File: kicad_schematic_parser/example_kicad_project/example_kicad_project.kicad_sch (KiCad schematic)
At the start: 0 parts

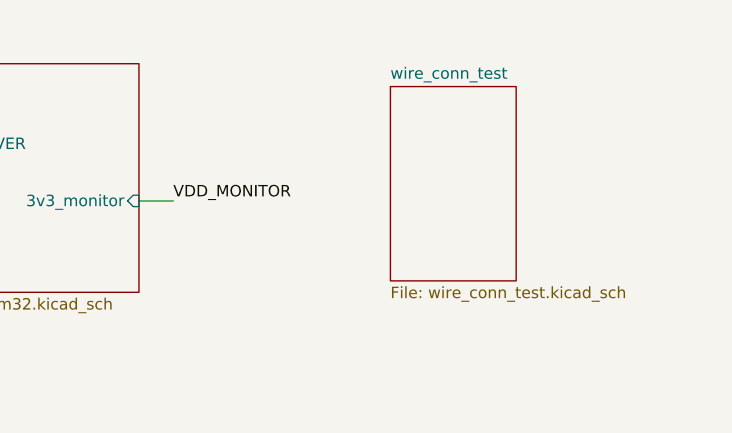
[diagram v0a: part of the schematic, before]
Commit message: sheets detecting component connections to pins
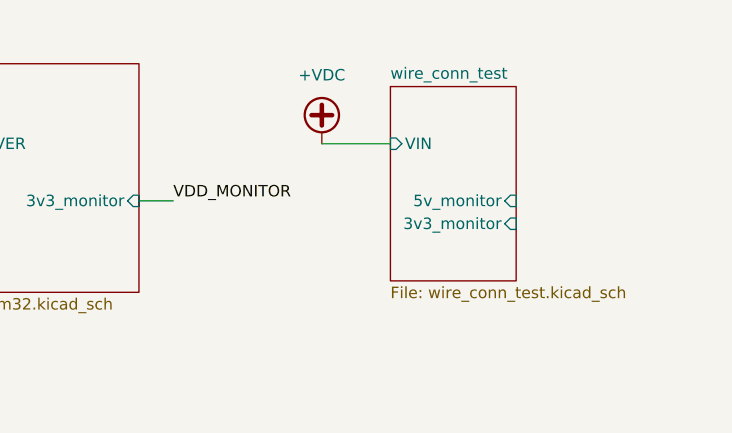
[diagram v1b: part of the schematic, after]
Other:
- sheet wire_conn_test ports: added 3v3_monitor, 5v_monitor, VIN; removed none
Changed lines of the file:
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@@
+	(wire
+		(pts
+			(xy 153.67 54.61) (xy 161.29 54.61)
+		)
+		(stroke
+			(width 0)
+			(type default)
+		)
+	)
 	(wire
 		(pts
@@
 			)
 			(justify left bottom)
+		)
+	)
+	(symbol
+		(lib_id "power:+VDC")
+		(at 153.67 54.61 0)
+		(unit 1)
+		(exclude_from_sim no)
+		(in_bom yes)
+		(on_board yes)
+		(dnp no)
+		(fields_autoplaced yes)
+		(property "Reference" "#PWR03"
+			(at 153.67 57.15 0)
+			(effects
+				(font
+					(size 1.27 1.27)
+				)
+				(hide yes)
+			)
+		)
+		(property "Value" "+VDC"
+			(at 153.67 46.99 0)
+			(effects
+				(font
+					(size 1.27 1.27)
+				)
+			)
+		)
+		(property "Footprint" ""
+			(at 153.67 54.61 0)
+			(effects
+				(font
+					(size 1.27 1.27)
+				)
+				(hide yes)
+			)
+		)
+		(property "Datasheet" ""
+			(at 153.67 54.61 0)
+			(effects
+				(font
+					(size 1.27 1.27)
+				)
+				(hide yes)
+			)
+		)
+		(property "Description" "Power symbol creates a global label with name \"+VDC\""
+			(at 153.67 54.61 0)
+			(effects
+				(font
+					(size 1.27 1.27)
+				)
+				(hide yes)
+			)
+		)
+		(pin "1"
+		)
+		(instances
+			(project ""
+				(path "/139408cf-b4ac-4ccf-8751-afbb6def1f13"
+					(reference "#PWR03")
+					(unit 1)
+				)
+			)
 		)
 	)
@@
 			)
 		)
+		(pin "VIN" input
+			(at 161.29 54.61 180)
+			(effects
+				(font
+					(size 1.27 1.27)
+				)
+				(justify left)
+			)
+		)
+		(pin "5v_monitor" input
+			(at 175.26 60.96 0)
+			(effects
+				(font
+					(size 1.27 1.27)
+				)
+				(justify right)
+			)
+		)
+		(pin "3v3_monitor" input
+			(at 175.26 63.5 0)
+			(effects
+				(font
+					(size 1.27 1.27)
+				)
+				(justify right)
+			)
+		)

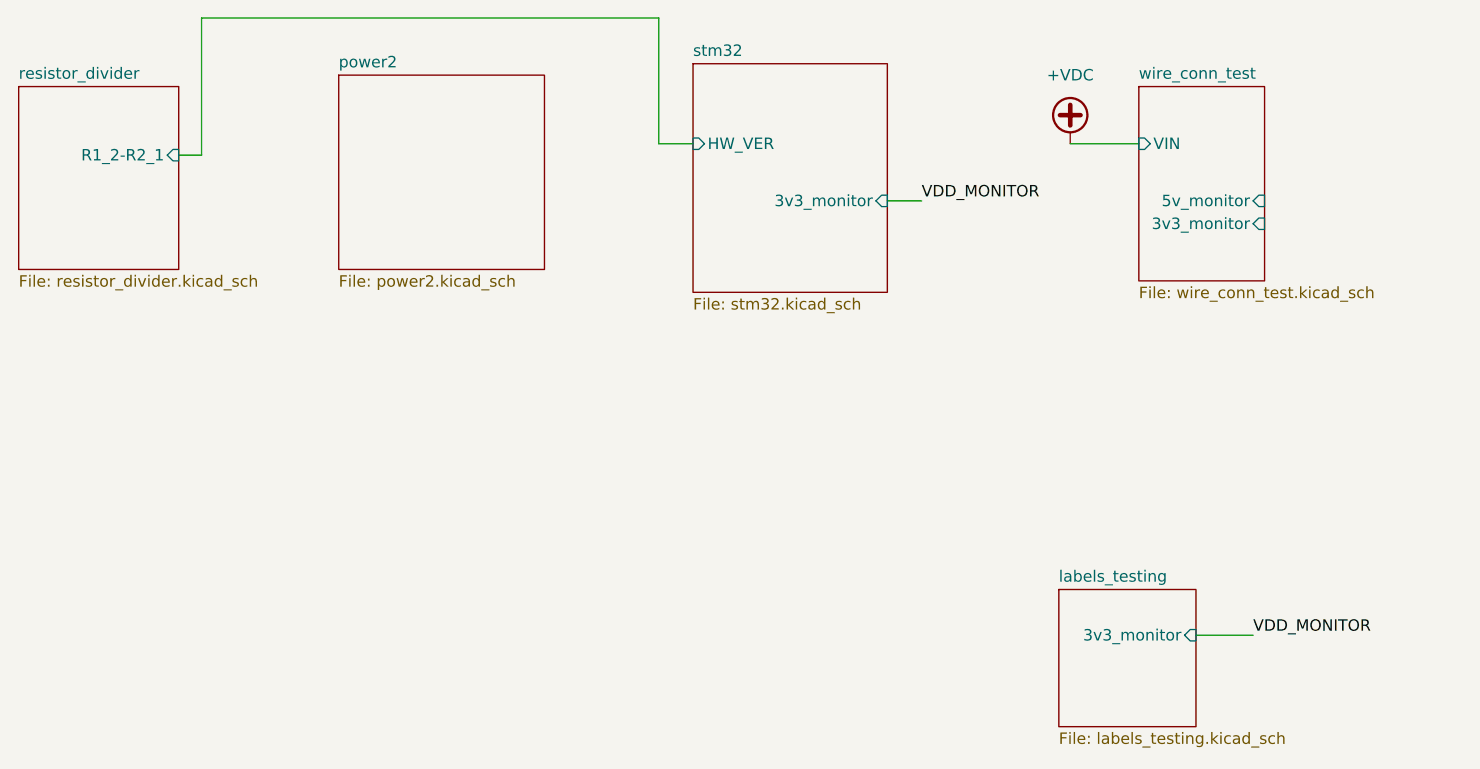
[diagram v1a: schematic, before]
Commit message: change to esp32 project, make more practical
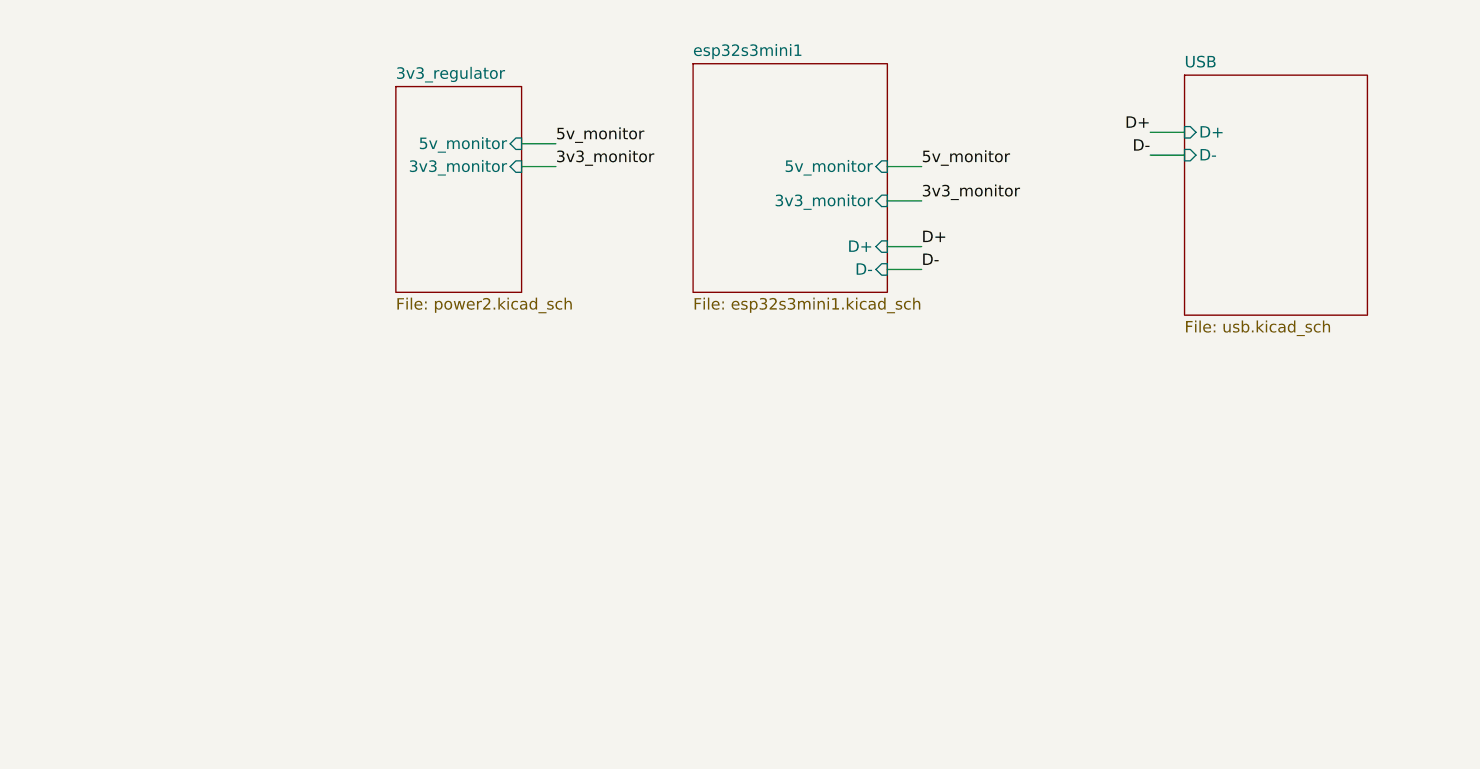
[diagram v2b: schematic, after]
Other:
- sheet stm32 renamed esp32s3mini1
- removed sheet labels_testing
- removed sheet power2
- removed sheet resistor_divider
- removed sheet wire_conn_test
- added sheet 3v3_regulator (power2.kicad_sch)
- added sheet USB (usb.kicad_sch)
- sheet esp32s3mini1: file stm32.kicad_sch -> esp32s3mini1.kicad_sch
- sheet esp32s3mini1 ports: added 5v_monitor, D+, D-; removed HW_VER
